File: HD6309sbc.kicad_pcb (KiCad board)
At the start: 2 copper layers, 99.8 x 99.8 mm, 32 parts, among them J1 Conn_01x02_Male, J2 Conn_02x30_Odd_Even, J3 Conn_01x02_Male, J4 Conn_01x06_Socket, J5 Conn_01x06_Socket, U1 HD63C09, U10 74LS375D, U11 74HC02, U12 74AHC1G08, U13 74HC21D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

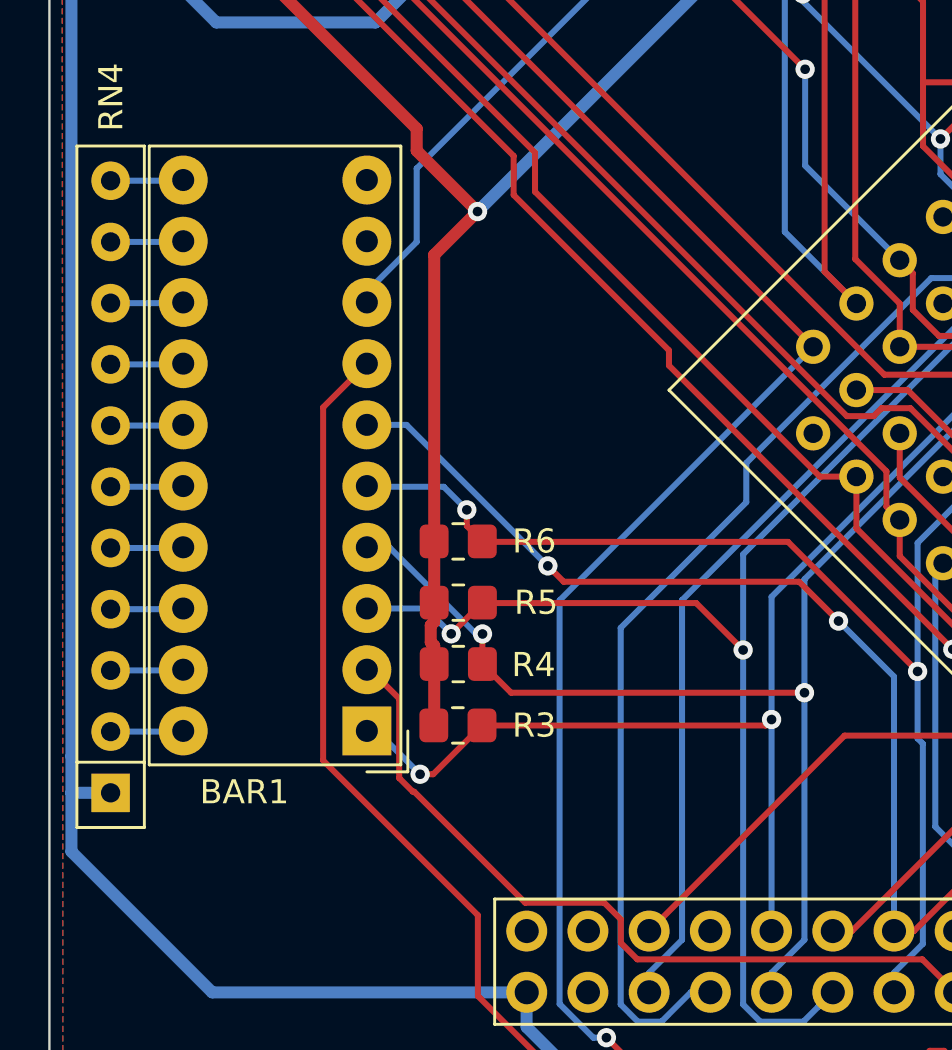
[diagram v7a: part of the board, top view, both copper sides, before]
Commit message: tidy up component placing
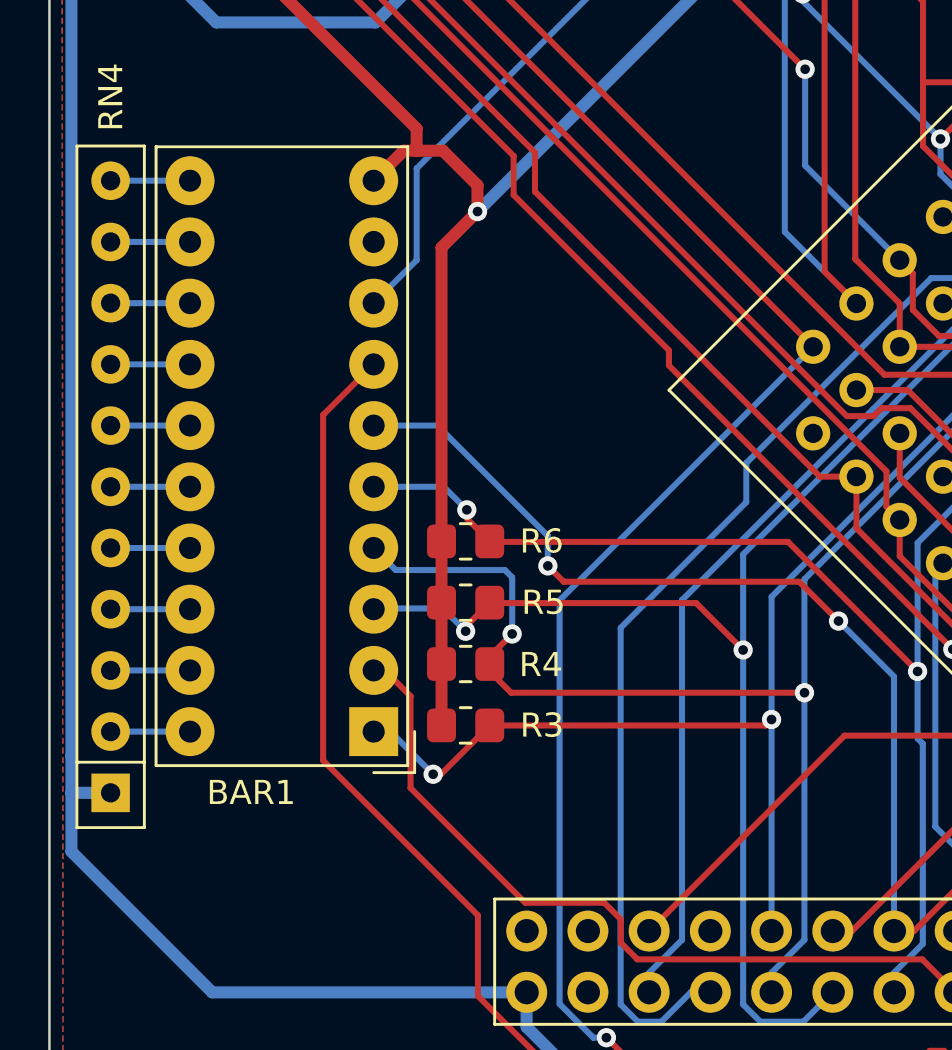
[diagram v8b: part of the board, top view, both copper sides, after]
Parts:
- moved R3 0.32 mm to (42.7, 109.0)
- moved R6 0.31 mm to (42.7, 101.3)
- moved R4 0.30 mm to (42.7, 106.4)
- moved R5 0.30 mm to (42.7, 103.9)
- moved BAR1 0.28 mm to (38.9, 109.2)
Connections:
- BAR1 pad 10: unconnected-(BAR1J-A-Pad10) -> +5V
- U15 pad 10: (no net) -> unconnected-(U15-Pad10)
- U15 pad 12: (no net) -> unconnected-(U15-Pad12)
- U15 pad 13: (no net) -> unconnected-(U15-Pad13)
- U15 pad 8: (no net) -> unconnected-(U15-Pad8)
- U15 pad 9: (no net) -> unconnected-(U15-Pad9)
- U7 pad 10: (no net) -> unconnected-(U7-Pad10)
- U7 pad 11: (no net) -> unconnected-(U7-Pad11)
- U7 pad 12: (no net) -> unconnected-(U7-Pad12)
- U7 pad 13: (no net) -> unconnected-(U7-Pad13)
- U8 pad 10: (no net) -> unconnected-(U8-Pad10)
- U8 pad 8: (no net) -> unconnected-(U8-Pad8)
- U8 pad 9: (no net) -> unconnected-(U8-Pad9)
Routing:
- net ~{IRQ}: track 62.0 -> 64.9 mm
- net +5V: track 519.3 -> 522.0 mm
